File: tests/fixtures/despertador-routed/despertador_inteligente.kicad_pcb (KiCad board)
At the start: 2 copper layers, 44 x 44 mm, 24 parts, among them J1 Conector ICSP, J2 CSE, U1 ATtiny85-20S, U2 MPU-6050, U3 MAX30102, U4 RFM69CW

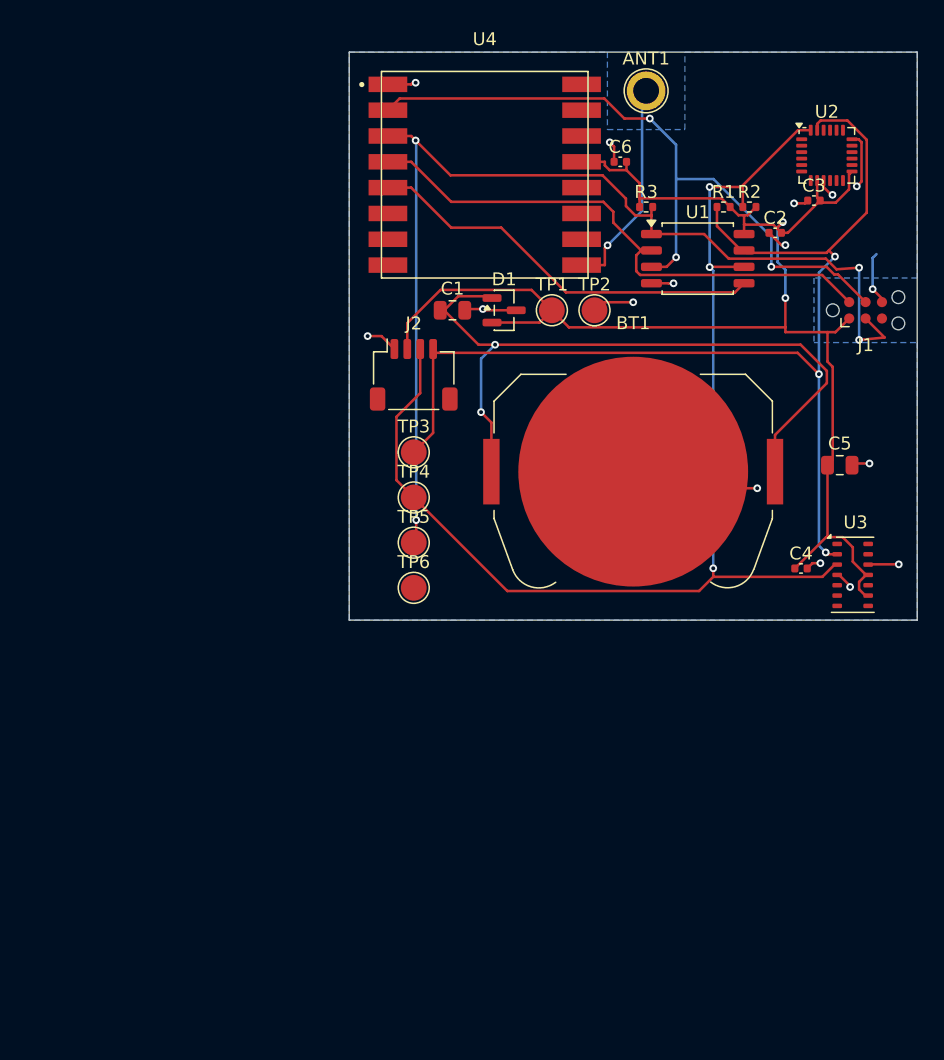
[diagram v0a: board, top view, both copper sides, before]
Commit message: test(fixtures): regenerar despertador-routed con ruteo de D5 (sesión 25)
Nueva colocación + ruteo desde cero sobre el mismo sch corregido de D3/D4.
DRC final 0/0, contrato D-23.2 verificado en las 3 corridas de route_board
usadas para generarlo (ver docs/historico/sesiones/25-reporte.md). Reemplaza
el fixture de sesión 20 (D3); el workaround manual de refill que ese README
documentaba como obligatorio ya no fue necesario.

Co-Authored-By: Claude Opus 5 <noreply@anthropic.com>
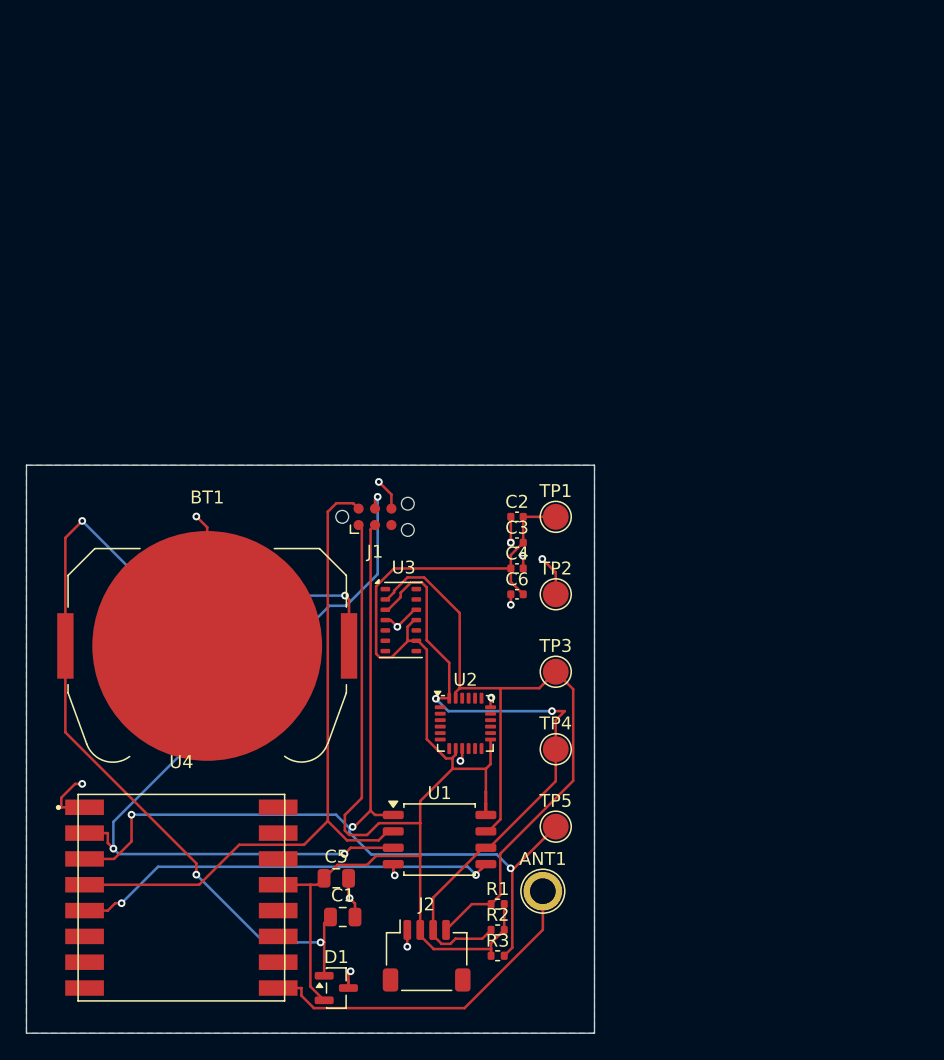
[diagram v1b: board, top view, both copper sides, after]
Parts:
- removed TP6: TestPoint, TestPoint:TestPoint_Pad_D2.0mm
- moved ANT1 62.5 mm to (165.0, 93.0)
- moved U4 60.7 mm to (137.0, 93.5)
- moved R2 59.3 mm to (161.5, 96.0)
- moved R3 59.1 mm to (161.5, 98.0)
- moved R1 56.8 mm to (161.5, 94.0)
- moved D1 54.1 mm to (149.0, 100.5)
- moved U2 52.2 mm to (159.0, 80.0)
- moved C5 50.4 mm to (149.0, 92.0)
- moved U1 49.2 mm to (157.0, 89.0)
- moved C1 47.8 mm to (149.5, 95.0)
- moved J2 45.0 mm to (156.0, 98.0)
- moved J1 41.2 mm to (152.0, 64.0)
- moved BT1 35.7 mm to (139.0, 74.0)
- moved U3 35.2 mm to (154.0, 72.0)
- moved C3 35.1 mm to (163.0, 66.0)
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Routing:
- net /SDA: track 93.7 -> 52.3 mm, vias 3 -> 2
- net /SCL: track 90.4 -> 59.7 mm, vias 3 -> 0
- net Net-(BT1-+): track 56.2 -> 75.7 mm, vias 2 -> 4
- net +3V3: track 112.7 -> 131.2 mm, vias 2 -> 0
- net /SCK: track 43.0 -> 53.7 mm
- net Net-(ANT1-A): track 16.6 -> 27.0 mm, vias 1 -> 0
- net GND: track 46.6 -> 37.6 mm, vias 16 -> 14
- net /MOSI: track 83.6 -> 75.8 mm, vias 4 -> 3
- net /MISO: track 55.1 -> 62.7 mm
- net /NSS: track 31.2 -> 33.6 mm, vias 0 -> 2

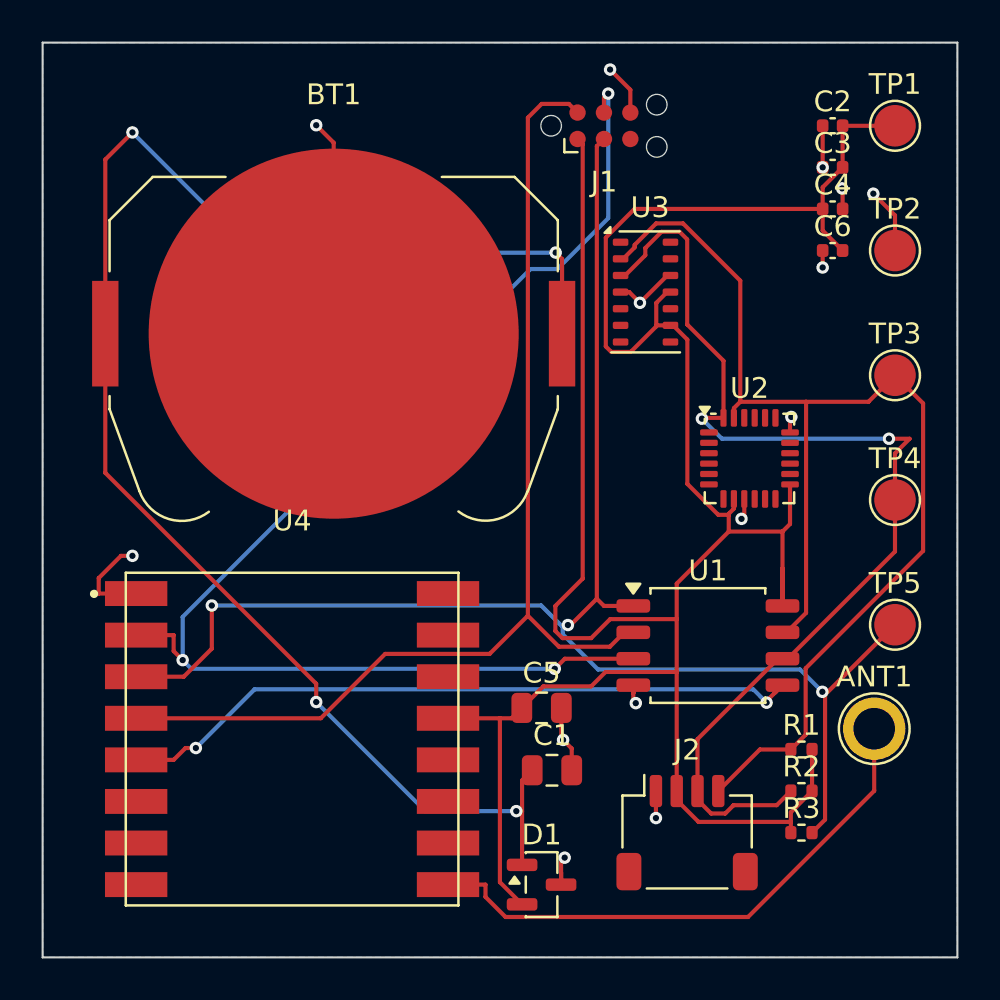
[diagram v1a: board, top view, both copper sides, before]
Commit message: test(fixtures): regenerar despertador-routed con ruteo de D6 (sesión 28)
Dogfooding 6 (segundo dogfooding de Fase 3): réplica exacta de la
colocación de D5 sobre board restaurado a estado pre-D3 (D-27.1), plano
GND + 3 corridas de route_board (1 completa + 2 re-ruteos parciales),
0 errores DRC en las 3. Solo .kicad_pcb cambió; sch/pro/prl
bit-idénticos a D5 (no se tocó esquemático ni configuración).

Co-Authored-By: Claude Sonnet 5 <noreply@anthropic.com>
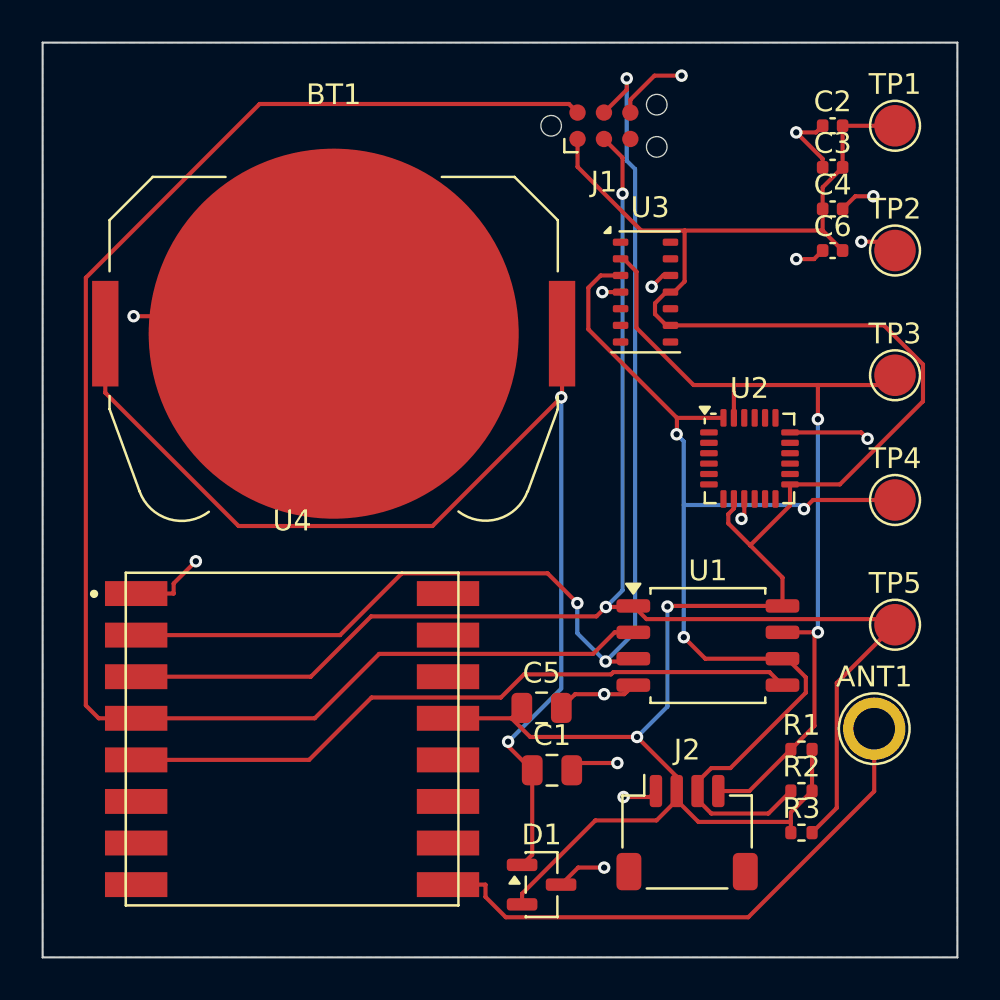
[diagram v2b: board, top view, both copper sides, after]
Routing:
- net /SCK: track 53.7 -> 76.2 mm
- net +3V3: track 131.2 -> 108.9 mm, vias 0 -> 2
- net Net-(BT1-+): track 75.7 -> 57.3 mm, vias 4 -> 2
- net /SCL: track 59.7 -> 43.1 mm, vias 0 -> 2
- net GND: track 37.6 -> 43.3 mm, vias 14 -> 15
- net /MISO: track 62.7 -> 58.8 mm
- net /MOSI: track 75.8 -> 73.2 mm, vias 3 -> 2
- net /SDA: track 52.3 -> 53.6 mm, vias 2 -> 3
- net /NSS: track 33.6 -> 33.1 mm, vias 2 -> 0

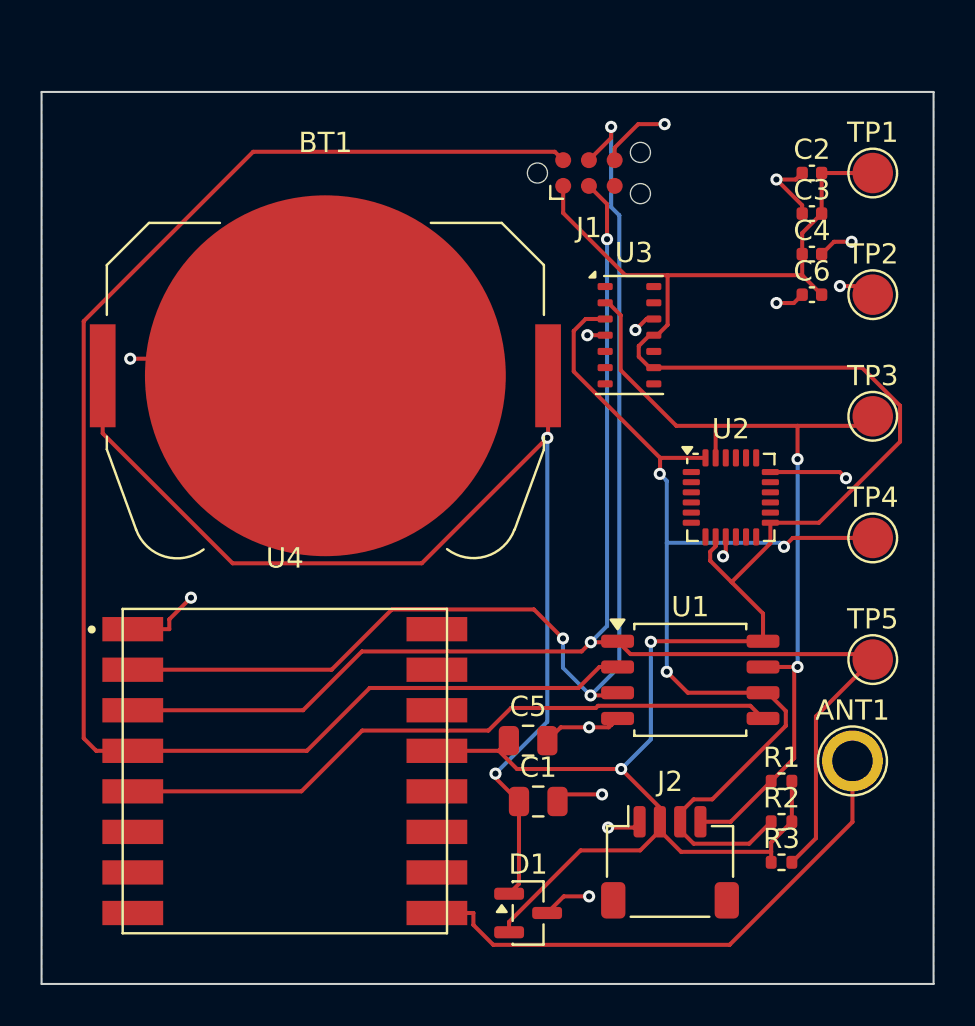
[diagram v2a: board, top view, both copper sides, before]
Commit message: test(fixtures): regenerar despertador-routed con ruteo de D7 (sesión 29)
Colocación con coordenadas propias (clusters funcionales en anti-diagonal,
distintas de D5/D6), plano GND creado antes de la colocación (D-28.1),
ruteo 10/10 nets sin errores DRC. Ver
tests/fixtures/despertador-routed/README.md para el detalle completo.

Co-Authored-By: Claude Sonnet 5 <noreply@anthropic.com>
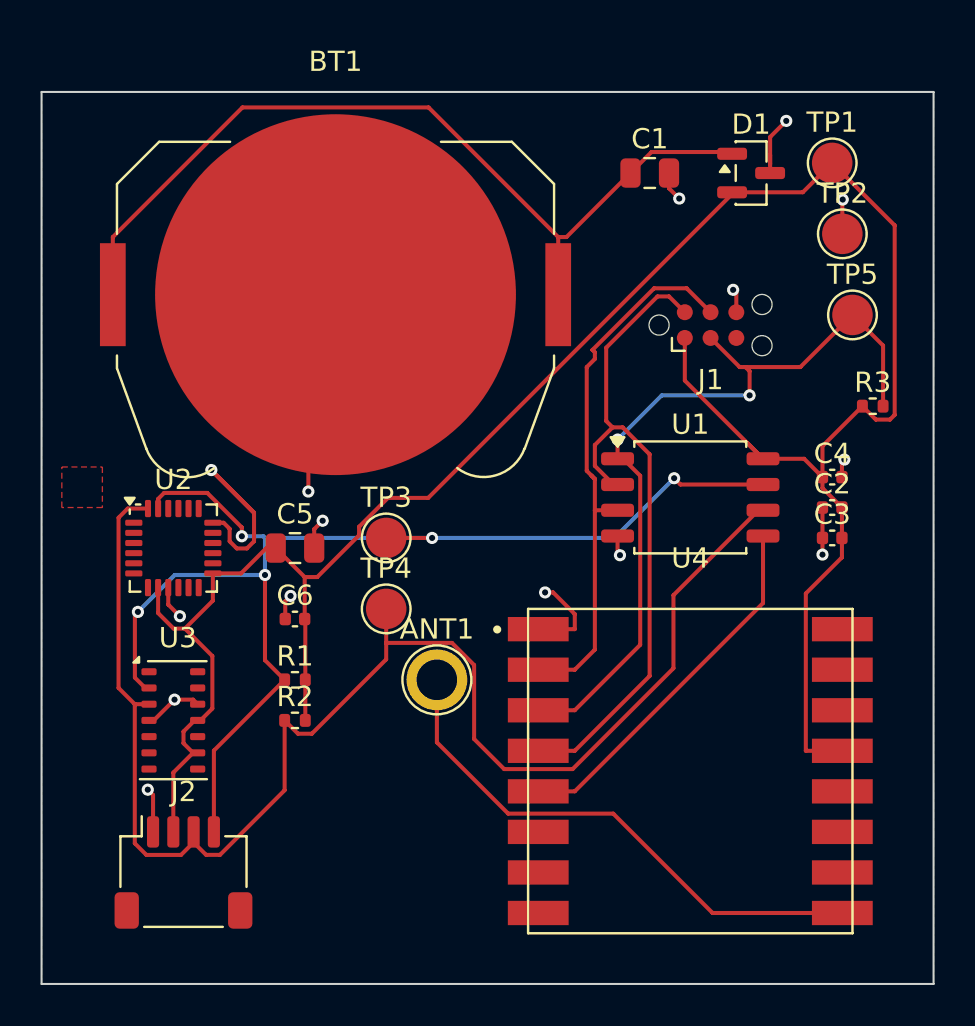
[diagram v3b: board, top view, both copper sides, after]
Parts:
- moved D1 38.1 mm to (160.0, 64.0)
- moved C1 31.5 mm to (155.0, 64.0)
- moved C6 30.1 mm to (137.5, 86.0)
- moved U3 29.4 mm to (131.5, 91.0)
- moved U2 27.6 mm to (131.5, 82.5)
- moved TP3 24.7 mm to (142.0, 82.0)
- moved R1 24.5 mm to (137.5, 89.0)
- moved R2 24.5 mm to (137.5, 91.0)
- moved TP4 24.3 mm to (142.0, 85.5)
- moved J2 24.0 mm to (132.0, 98.5)
- moved R3 22.9 mm to (166.0, 75.5)
- moved ANT1 20.9 mm to (144.5, 89.0)
- moved U4 20.0 mm to (157.0, 93.5)
- moved TP5 17.0 mm to (165.0, 71.0)
- moved C2 16.5 mm to (164.0, 80.5)
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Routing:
- net /SCK: track 76.2 -> 33.5 mm
- net /MOSI: track 73.2 -> 39.8 mm
- net /MISO: track 58.8 -> 27.3 mm, vias 3 -> 0
- net /SCL: track 43.1 -> 62.8 mm, vias 2 -> 5
- net /SDA: track 53.6 -> 72.2 mm, vias 3 -> 0
- net /NSS: track 33.1 -> 18.2 mm
- net Net-(BT1-+): track 57.3 -> 43.3 mm, vias 2 -> 0
- net GND: track 43.3 -> 50.0 mm
- net +3V3: track 108.9 -> 114.2 mm, vias 2 -> 0
- added copper zone on F.Cu, net GND
